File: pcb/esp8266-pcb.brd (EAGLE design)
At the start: 45.7 x 45.7 mm, 17 parts

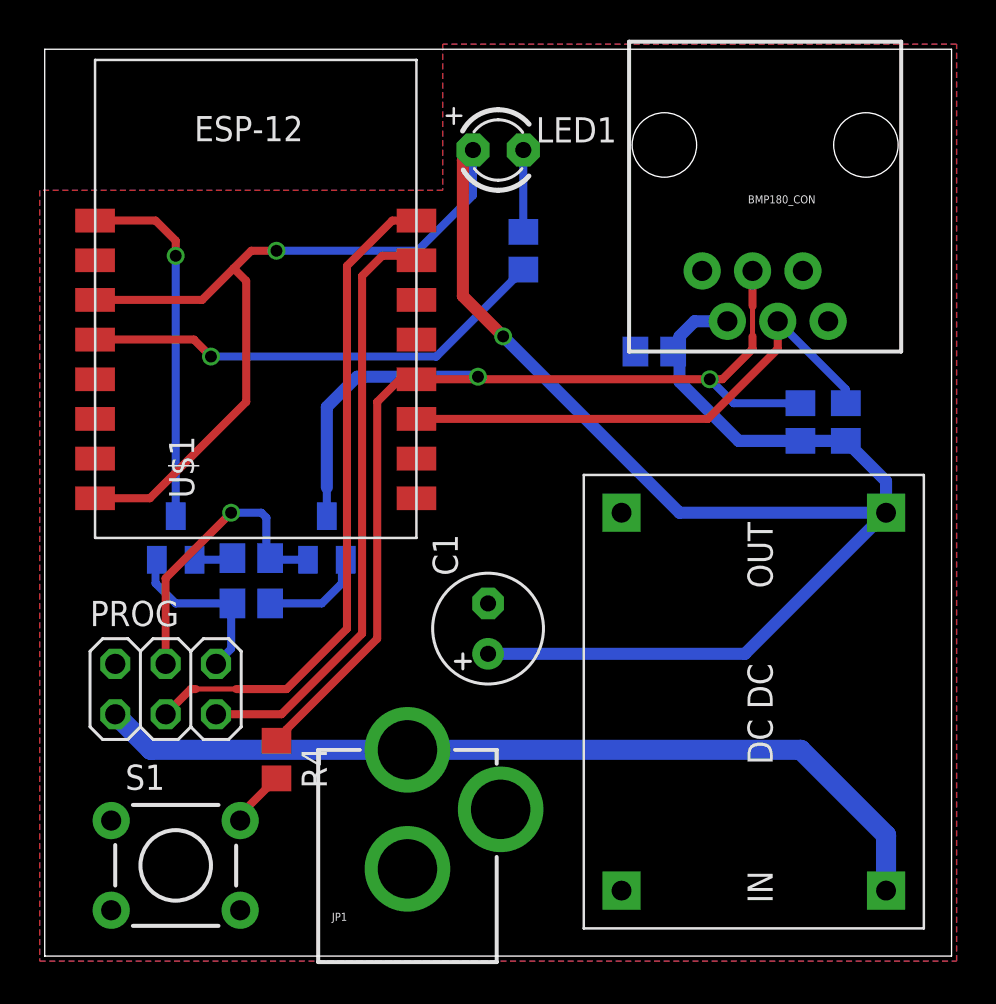
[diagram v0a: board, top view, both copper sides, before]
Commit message: Added mount holes.
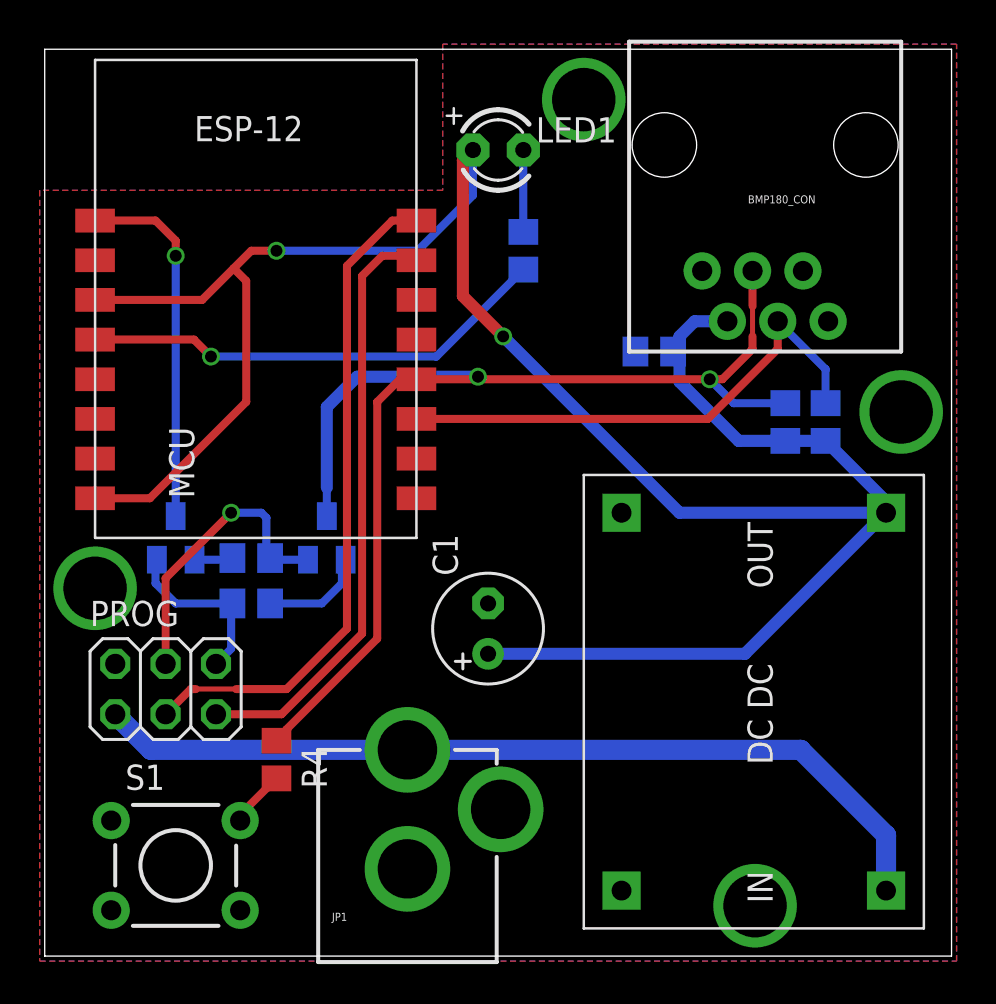
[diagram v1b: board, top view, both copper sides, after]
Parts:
- moved R5 1.02 mm to (39.4, 26.9)
- moved R6 0.76 mm to (37.3, 26.9)
- renumbered U$1 to MCU
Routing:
- net GPIO0: track 62.2 -> 61.4 mm
- net +3V3: track 116.0 -> 115.4 mm
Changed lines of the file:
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@@
 <element name="S1" library="SparkFun-Retired" package="TACTILE-PTH" value="" x="6.604" y="4.572"/>
 <element name="C2" library="rcl" package="C0805" value="100nF" x="30.734" y="30.48" rot="MR0"/>
-<element name="U$1" library="ESP8266-ESP12" package="ESP8266-ESP12" value="ESP8266_ESP-12" x="2.54" y="21.082"/>
+<element name="MCU" library="ESP8266-ESP12" package="ESP8266-ESP12" value="ESP8266_ESP-12" x="2.54" y="21.082"/>
 <element name="R1" library="rcl" package="R0805" value="??R" x="24.13" y="35.56" rot="MR270"/>
 <element name="T1" library="transistor" package="SOT23-BEC" value="" x="14.224" y="21.082" rot="MR0"/>
@@
 <element name="PROG" library="pinhead" package="2X03" value="" x="6.096" y="13.462"/>
 <element name="R4" library="rcl" package="R0805" value="470" x="11.684" y="9.906" rot="R270"/>
-<element name="R5" library="rcl" package="R0805" value="10k" x="40.386" y="26.924" rot="MR270"/>
-<element name="R6" library="rcl" package="R0805" value="10k" x="38.1" y="26.924" rot="MR270"/>
+<element name="R5" library="rcl" package="R0805" value="10k" x="39.37" y="26.924" rot="MR270"/>
+<element name="R6" library="rcl" package="R0805" value="10k" x="37.338" y="26.924" rot="MR270"/>
 </elements>
 <signals>
@@
 <contactref element="S1" pad="3"/>
 <contactref element="S1" pad="4"/>
-<contactref element="U$1" pad="1"/>
+<contactref element="MCU" pad="1"/>
 <contactref element="JP1" pad="GNDBREAK"/>
 <contactref element="JP1" pad="GND"/>
@@
 <vertex x="20.066" y="38.608"/>
 </polygon>
+<via x="27.178" y="43.18" extent="1-16" drill="3.2"/>
+<via x="43.18" y="27.432" extent="1-16" drill="3.2"/>
+<via x="35.814" y="2.54" extent="1-16" drill="3.2"/>
+<via x="2.54" y="18.542" extent="1-16" drill="3.2"/>
 </signal>
 <signal name="N$1">
@@
 </signal>
 <signal name="+3V3">
-<contactref element="U$1" pad="11"/>
-<contactref element="U$1" pad="16"/>
+<contactref element="MCU" pad="11"/>
+<contactref element="MCU" pad="16"/>
 <contactref element="BMP180_CON" pad="5"/>
 <contactref element="C2" pad="1"/>
@@
 <wire x1="2.54" y1="33.082" x2="7.936" y2="33.082" width="0.4064" layer="1"/>
 <wire x1="21.59" y1="40.64" x2="21.59" y2="38.354" width="0.4064" layer="16"/>
-<wire x1="42.418" y1="22.352" x2="42.418" y2="23.942" width="0.6096" layer="16"/>
-<wire x1="42.418" y1="23.942" x2="40.386" y2="25.974" width="0.6096" layer="16"/>
-<wire x1="40.386" y1="25.974" x2="38.1" y2="25.974" width="0.6096" layer="16"/>
-<wire x1="38.1" y1="25.974" x2="34.986" y2="25.974" width="0.6096" layer="16"/>
+<wire x1="39.37" y1="25.974" x2="37.338" y2="25.974" width="0.6096" layer="16"/>
+<wire x1="37.338" y1="25.974" x2="34.986" y2="25.974" width="0.6096" layer="16"/>
 <wire x1="34.986" y1="25.974" x2="32.004" y2="28.956" width="0.6096" layer="16"/>
 <wire x1="32.766" y1="32.004" x2="34.417" y2="32.004" width="0.6096" layer="16"/>
@@
 <wire x1="21.082" y1="33.274" x2="21.082" y2="40.132" width="0.6096" layer="1"/>
 <wire x1="21.082" y1="40.132" x2="21.59" y2="40.64" width="0.6096" layer="1"/>
+<wire x1="42.418" y1="22.352" x2="42.418" y2="22.926" width="0.6096" layer="16"/>
+<wire x1="42.418" y1="22.926" x2="39.37" y2="25.974" width="0.6096" layer="16"/>
 </signal>
 <signal name="N$3">
@@
 <signal name="TXD">
 <contactref element="PROG" pad="3"/>
-<contactref element="U$1" pad="8"/>
+<contactref element="MCU" pad="8"/>
 <wire x1="6.096" y1="12.192" x2="7.366" y2="13.462" width="0.4064" layer="1"/>
 <wire x1="7.366" y1="13.462" x2="7.62" y2="13.462" width="0.4064" layer="1"/>
@@
 <signal name="RXD">
 <contactref element="PROG" pad="5"/>
-<contactref element="U$1" pad="7"/>
+<contactref element="MCU" pad="7"/>
 <wire x1="18.74" y1="35.082" x2="18.74" y2="35.25" width="0.4064" layer="1"/>
 <wire x1="18.74" y1="35.25" x2="18.796" y2="35.306" width="0.4064" layer="1"/>
@@
 <signal name="NRST">
 <contactref element="T2" pad="C"/>
-<contactref element="U$1" pad="9"/>
+<contactref element="MCU" pad="9"/>
 <wire x1="6.604" y1="22.182" x2="6.604" y2="35.306" width="0.4064" layer="16"/>
 <wire x1="2.54" y1="37.082" x2="5.59" y2="37.082" width="0.4064" layer="1"/>
@@
 <contactref element="BMP180_CON" pad="4"/>
 <contactref element="R6" pad="1"/>
-<contactref element="U$1" pad="4"/>
+<contactref element="MCU" pad="4"/>
 <wire x1="14.224" y1="22.182" x2="14.224" y2="23.622" width="0.4064" layer="16"/>
 <wire x1="35.687" y1="34.544" x2="35.687" y2="32.766" width="0.4064" layer="1"/>
@@
 <wire x1="35.687" y1="31.242" x2="35.687" y2="30.607" width="0.4064" layer="1"/>
 <wire x1="35.687" y1="30.607" x2="34.162" y2="29.082" width="0.4064" layer="1"/>
-<wire x1="18.74" y1="29.082" x2="19.260146875" y2="29.082" width="0.4064" layer="1"/>
 <wire x1="21.716" y1="29.082" x2="33.528" y2="29.082" width="0.4064" layer="1"/>
 <wire x1="33.528" y1="29.082" x2="34.162" y2="29.082" width="0.4064" layer="1"/>
@@
 <wire x1="12.192" y1="11.43" x2="12.192" y2="11.364" width="0.4064" layer="1"/>
 <wire x1="12.192" y1="11.364" x2="11.684" y2="10.856" width="0.4064" layer="1"/>
-<wire x1="38.1" y1="27.874" x2="34.736" y2="27.874" width="0.4064" layer="16"/>
+<wire x1="37.338" y1="27.874" x2="34.736" y2="27.874" width="0.4064" layer="16"/>
 <wire x1="34.736" y1="27.874" x2="33.528" y2="29.082" width="0.4064" layer="16"/>
 <via x="33.528" y="29.082" extent="1-16" drill="0.6"/>
 <wire x1="14.224" y1="23.622" x2="14.224" y2="27.686" width="0.6096" layer="16"/>
-<wire x1="19.260146875" y1="29.082" x2="21.716" y2="29.082" width="0.4064" layer="1"/>
+<wire x1="18.74" y1="29.082" x2="21.716" y2="29.082" width="0.4064" layer="1"/>
 <wire x1="21.716" y1="29.082" x2="21.844" y2="29.21" width="0.4064" layer="1"/>
 <via x="21.844" y="29.21" extent="1-16" drill="0.6"/>
@@
 <contactref element="BMP180_CON" pad="3"/>
 <contactref element="R5" pad="1"/>
-<contactref element="U$1" pad="3"/>
+<contactref element="MCU" pad="3"/>
 <wire x1="18.74" y1="27.082" x2="33.432" y2="27.082" width="0.4064" layer="1"/>
 <wire x1="33.432" y1="27.082" x2="36.957" y2="30.607" width="0.4064" layer="1"/>
 <wire x1="36.957" y1="32.004" x2="36.957" y2="30.607" width="0.4064" layer="1"/>
-<wire x1="40.386" y1="27.874" x2="40.386" y2="28.575" width="0.4064" layer="16"/>
-<wire x1="40.386" y1="28.575" x2="36.957" y2="32.004" width="0.4064" layer="16"/>
+<wire x1="39.37" y1="27.874" x2="39.37" y2="29.591" width="0.4064" layer="16"/>
+<wire x1="39.37" y1="29.591" x2="36.957" y2="32.004" width="0.4064" layer="16"/>
 </signal>
 <signal name="GPIO13">
-<contactref element="U$1" pad="15"/>
+<contactref element="MCU" pad="15"/>
 </signal>
 <signal name="GPIO12">
-<contactref element="U$1" pad="14"/>
+<contactref element="MCU" pad="14"/>
 </signal>
 <signal name="GPIO16">
 <contactref element="R1" pad="2"/>
-<contactref element="U$1" pad="12"/>
+<contactref element="MCU" pad="12"/>
 <wire x1="2.54" y1="31.082" x2="7.526" y2="31.082" width="0.4064" layer="1"/>
 <wire x1="7.526" y1="31.082" x2="8.382" y2="30.226" width="0.4064" layer="1"/>

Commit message: Rearanged bNames and tNames.
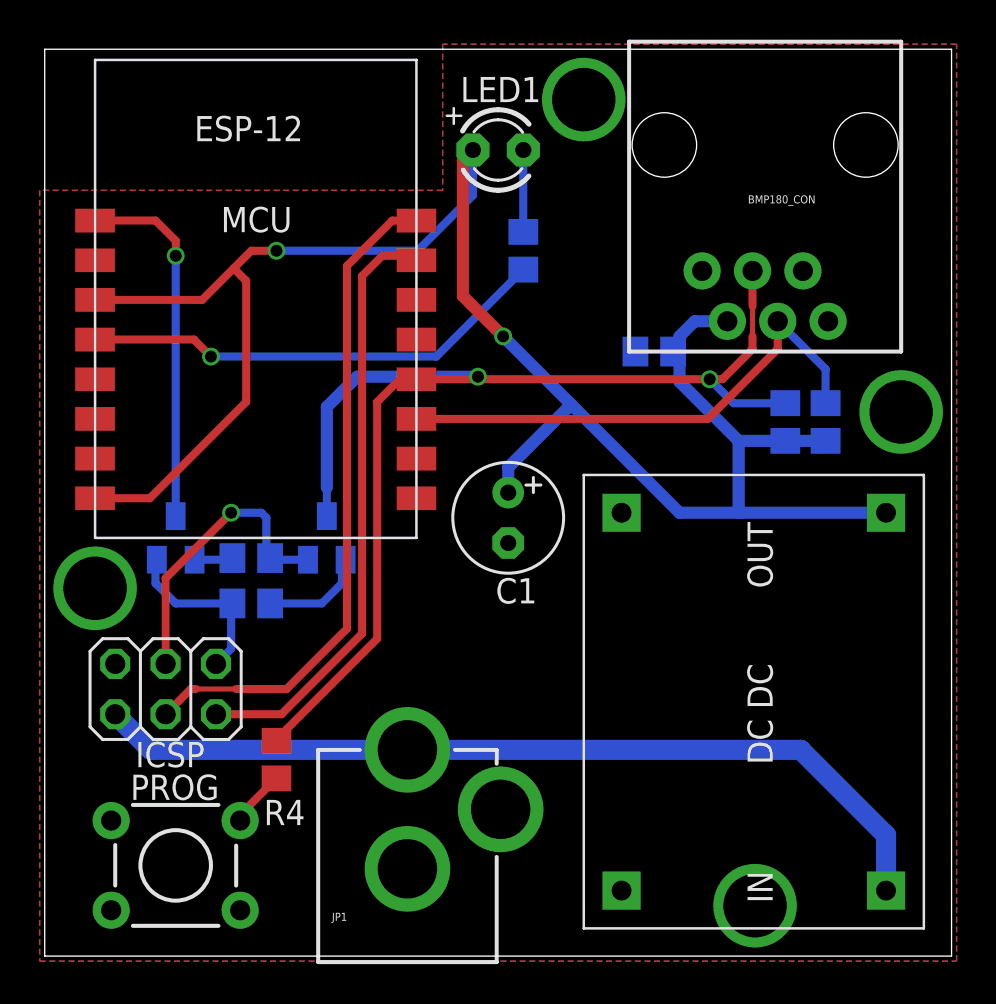
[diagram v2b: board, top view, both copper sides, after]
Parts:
- removed S1: (no value), SparkFun-Retired:TACTILE-PTH
- added ICSP: (no value), pinhead:2X03
- PROG: device pinhead:2X03 -> SparkFun-Retired:TACTILE-PTH
- moved PROG 8.90 mm to (6.60, 4.57)
- moved C1 5.68 mm to (23.4, 22.1), turned to 270 degrees
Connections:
- net DTR: now also ICSP.4; no longer PROG.4
- net GND: now also ICSP.2, PROG.3, PROG.4; no longer PROG.2, S1.3, S1.4
- net N$4: now also PROG.2; no longer S1.2
- net RST: now also ICSP.6; no longer PROG.6
- net RXD: now also ICSP.5; no longer PROG.5
- net TXD: now also ICSP.3; no longer PROG.3
- net VIN: now also ICSP.1; no longer PROG.1
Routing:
- net +3V3: track 115.4 -> 96.9 mm
